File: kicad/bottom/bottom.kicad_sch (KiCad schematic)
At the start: 17 parts, among them J1 Conn_01x15_Socket

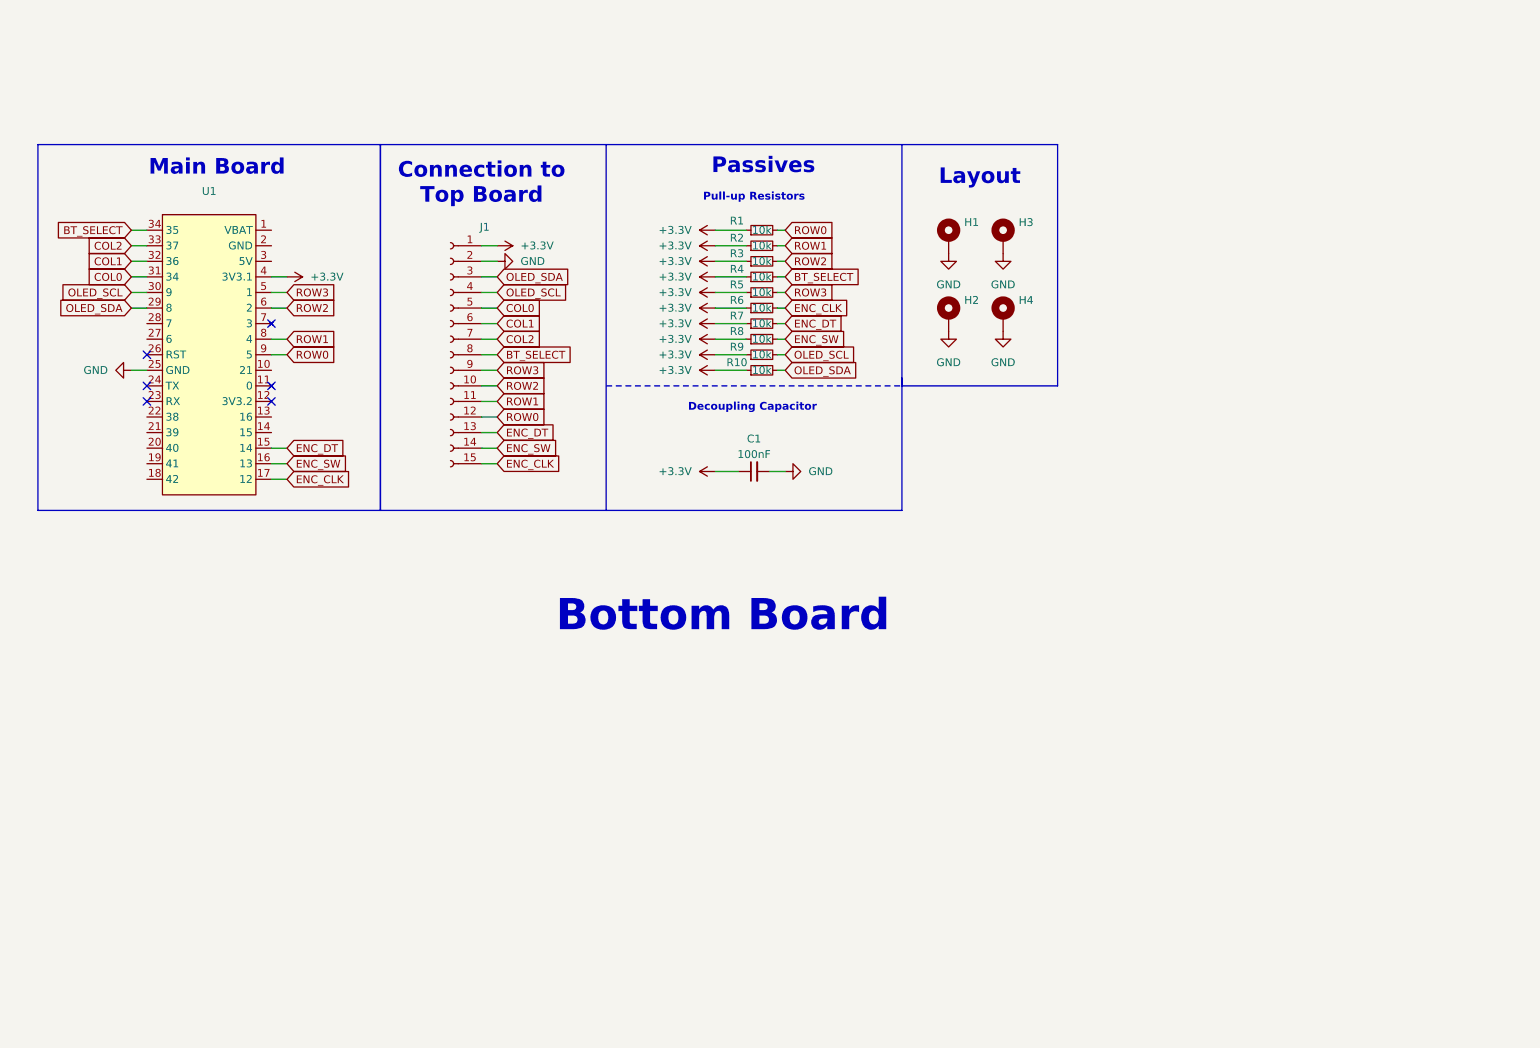
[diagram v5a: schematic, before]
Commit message: update imports, readme, documentatie, add 10 addressable rgbs
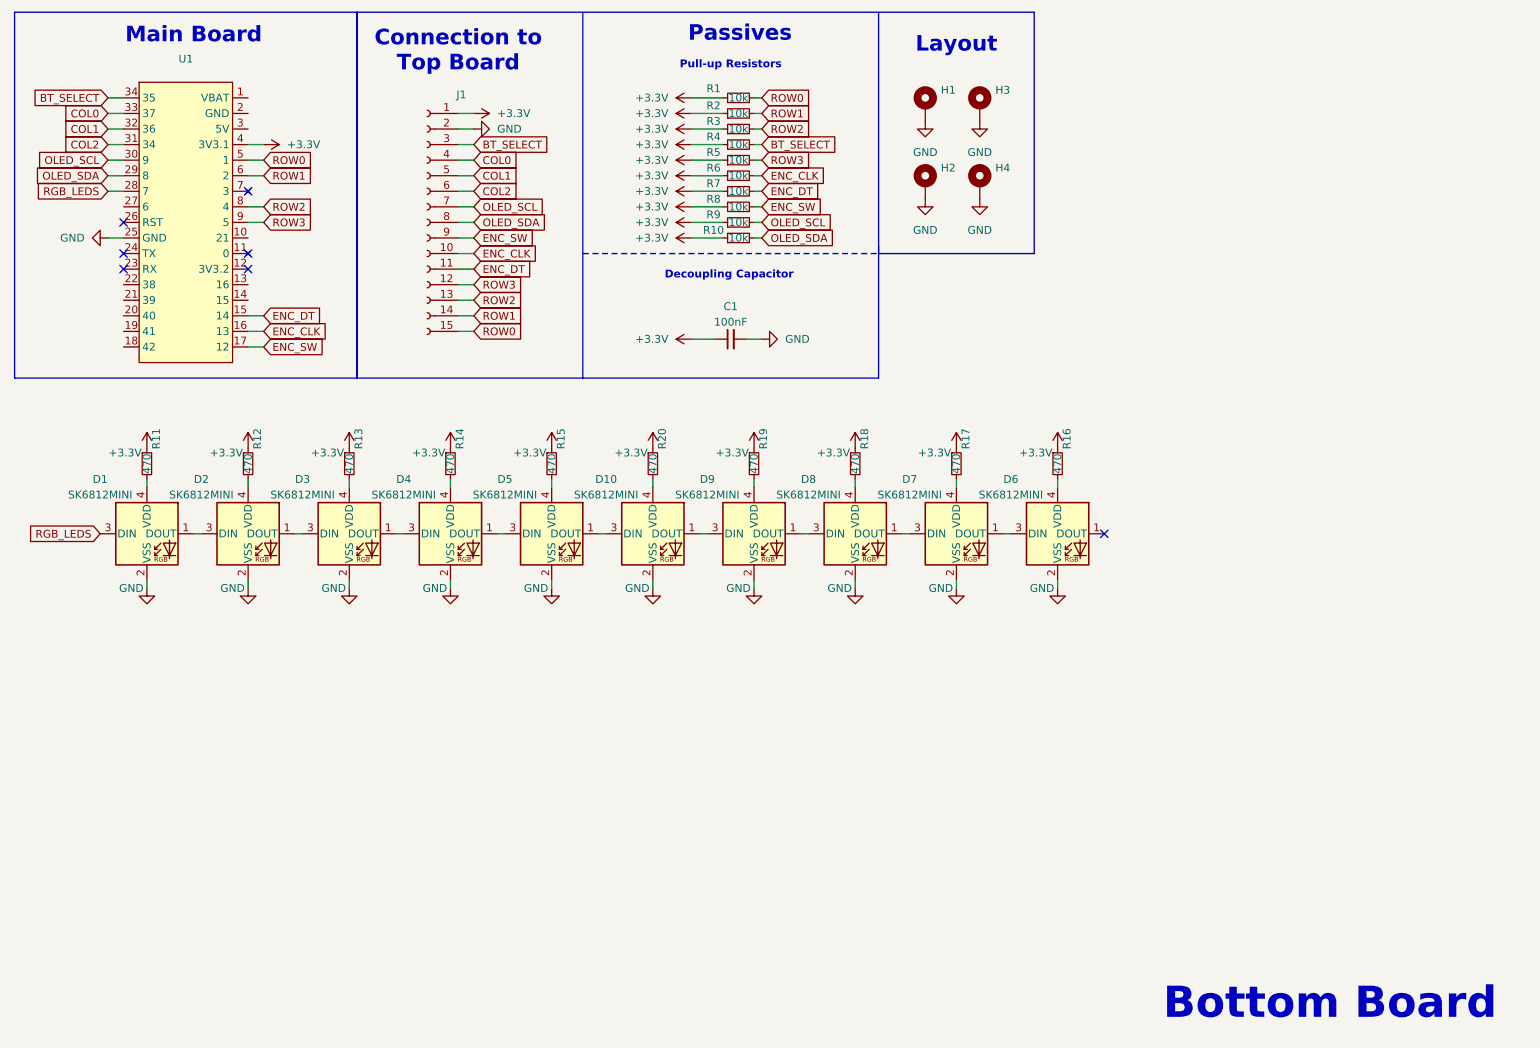
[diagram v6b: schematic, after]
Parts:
- added D1, D10, D2, D3, D4, D5, D6, D7, D8, D9: SK6812MINI, Bottom-Footprints:LED_SK6812MINI_PLCC4_3.5x3.5mm_P1.75mm, symbol Bottom-Symbols:SK6812MINI
- added R11, R12, R13, R14, R15, R16, R17, R18, R19, R20: 470, Bottom-Footprints:R_0805_2012Metric_Pad1.20x1.40mm_HandSolder, symbol Bottom-Symbols:R_Small
- C1: footprint Bottom-Footprints:C_1206_3216Metric_Pad1.33x1.80mm_HandSolder -> Bottom-Footprints:C_0805_2012Metric_Pad1.18x1.45mm_HandSolder
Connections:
- net +3.3V: now also R11.1, R12.1, R13.1, R14.1, R15.1, R16.1, R17.1, R18.1, R19.1, R20.1
- net BT_SELECT: now also J1.3 (Pin_3); no longer J1.8 (Pin_8)
- net COL0: now also J1.4 (Pin_4), U1.33 (37); no longer J1.5 (Pin_5), U1.31 (34)
- net COL1: now also J1.5 (Pin_5); no longer J1.6 (Pin_6)
- net COL2: now also J1.6 (Pin_6), U1.31 (34); no longer J1.7 (Pin_7), U1.33 (37)
- net ENC_CLK: now also J1.10 (Pin_10), U1.16 (13); no longer J1.15 (Pin_15), U1.17 (12)
- net ENC_DT: now also J1.11 (Pin_11); no longer J1.13 (Pin_13)
- net ENC_SW: now also J1.9 (Pin_9), U1.17 (12); no longer J1.14 (Pin_14), U1.16 (13)
- net GND: now also D1.2 (VSS), D10.2 (VSS), D2.2 (VSS), D3.2 (VSS), D4.2 (VSS), D5.2 (VSS), D6.2 (VSS), D7.2 (VSS), D8.2 (VSS), D9.2 (VSS)
- net OLED_SCL: now also J1.7 (Pin_7); no longer J1.4 (Pin_4)
- net OLED_SDA: now also J1.8 (Pin_8); no longer J1.3 (Pin_3)
- net ROW0: now also J1.15 (Pin_15), U1.5 (1); no longer J1.12 (Pin_12), U1.9 (5)
- net ROW1: now also J1.14 (Pin_14), U1.6 (2); no longer J1.11 (Pin_11), U1.8 (4)
- net ROW2: now also J1.13 (Pin_13), U1.8 (4); no longer J1.10 (Pin_10), U1.6 (2)
- net ROW3: now also J1.12 (Pin_12), U1.9 (5); no longer J1.9 (Pin_9), U1.5 (1)
- net RGB_LEDS: now reaches U1.28 (7)
- net RGB_LEDS: now also D1.3 (DIN)
- new net: D1.1 (DOUT), D2.3 (DIN)
- new net: D1.4 (VDD), R11.2
- new net: D7.3 (DIN), D8.1 (DOUT)
- new net: D8.3 (DIN), D9.1 (DOUT)
- new net: D8.4 (VDD), R18.2
- new net: D4.4 (VDD), R14.2
- new net: D10.4 (VDD), R20.2
- new net: D6.3 (DIN), D7.1 (DOUT)
- new net: D7.4 (VDD), R17.2
- new net: D4.1 (DOUT), D5.3 (DIN)
- new net: D3.1 (DOUT), D4.3 (DIN)
- new net: D3.4 (VDD), R13.2
- new net: D10.1 (DOUT), D9.3 (DIN)
- new net: D10.3 (DIN), D5.1 (DOUT)
- new net: D2.1 (DOUT), D3.3 (DIN)
- new net: D2.4 (VDD), R12.2
- new net: D6.4 (VDD), R16.2
- new net: D5.4 (VDD), R15.2
- new net: D9.4 (VDD), R19.2
- no-connect marks 6 -> 7
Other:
- moved on the sheet: C1, H1, H2, H3, H4, J1, R1, R10, R2, R3, R4, R5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

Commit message: Update KiCad project files and documentation
- Adjusted pad dimensions in top.kicad_pro:
  - Drill size changed from 1.0 to 0.8
  - Height changed from 1.7 to 1.6
  - Width changed from 1.7 to 2.0
- Modified design rule for isolated copper from "warning" to "ignore"
- Increased minimum hole clearance from 0.16 to 0.25

- Corrected global label positions for OLED_SDA and OLED_SCL in top.kicad_sch
- Updated footprint properties for mounting holes in top.kicad_sch to "MountingHole:MountingHole_2.5mm_Pad"

- Created new documentation file for component details.
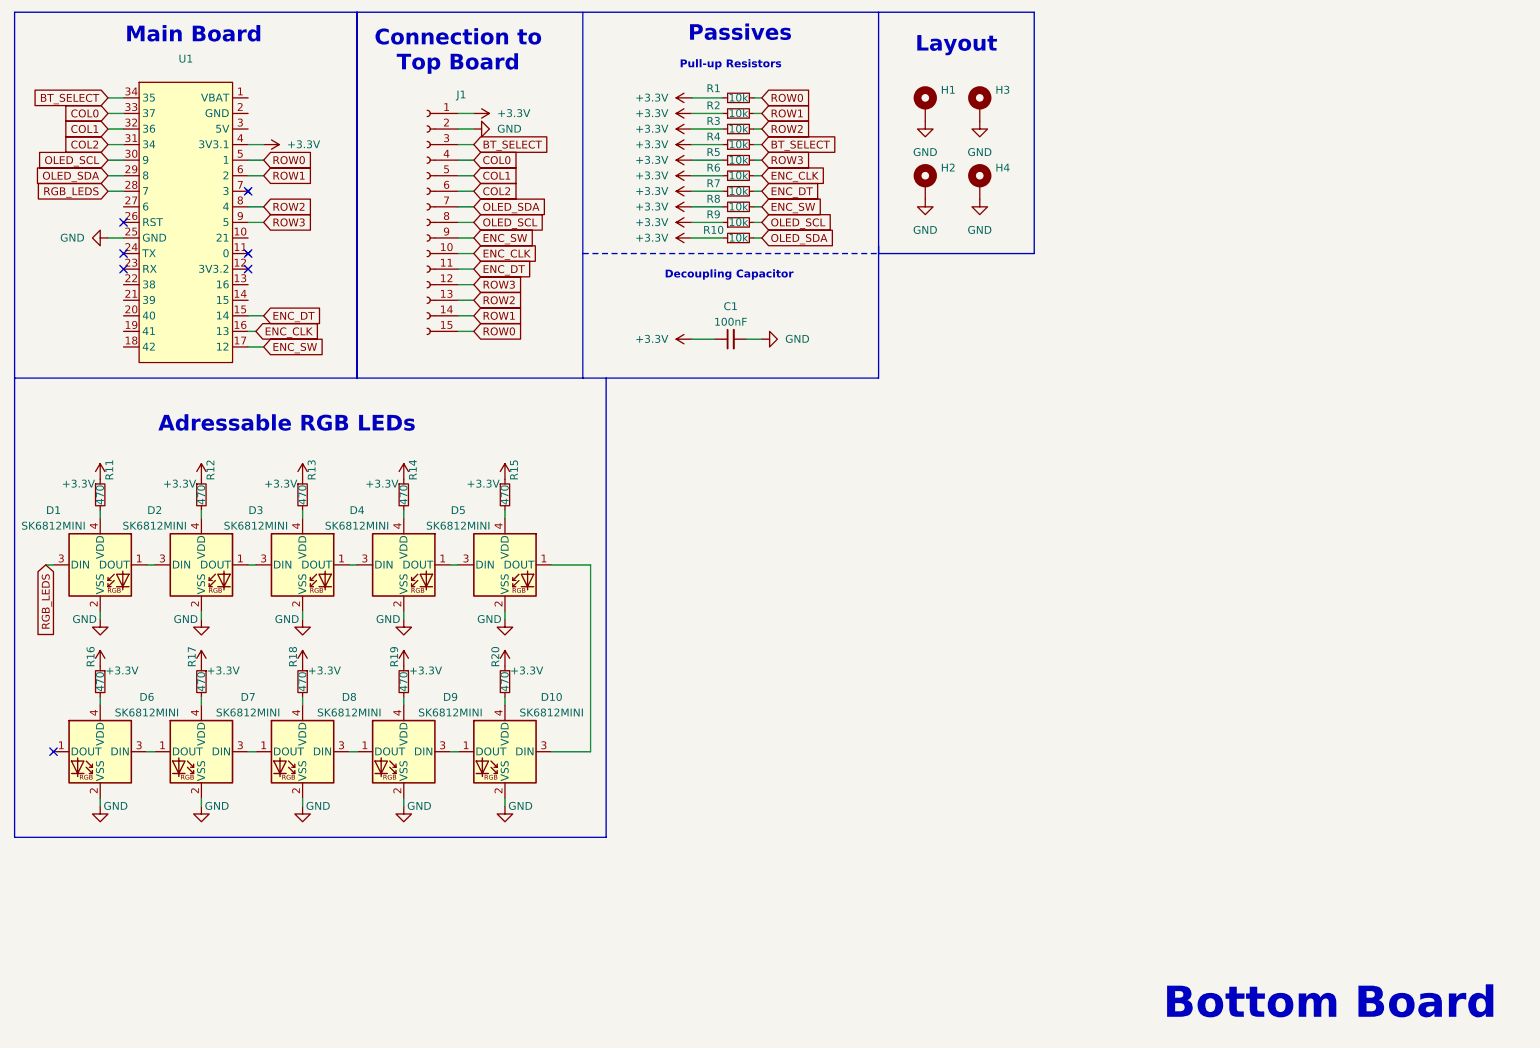
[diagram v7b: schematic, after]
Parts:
- H1, H2, H3, H4: footprint Bottom-Footprints:MountingHole_2.2mm_M2_DIN965_Pad -> MountingHole:MountingHole_2.5mm_Pad
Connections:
- net OLED_SCL: now also J1.8 (Pin_8); no longer J1.7 (Pin_7)
- net OLED_SDA: now also J1.7 (Pin_7); no longer J1.8 (Pin_8)
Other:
- note added: "Adressable RGB LEDs"
- moved on the sheet: D1, D10, D2, D3, D4, D5, D6, D7, D8, D9, R11, R12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
